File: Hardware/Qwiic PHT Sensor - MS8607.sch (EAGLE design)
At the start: 21 parts, among them J3 PTH, U1 MS8607-02BA01

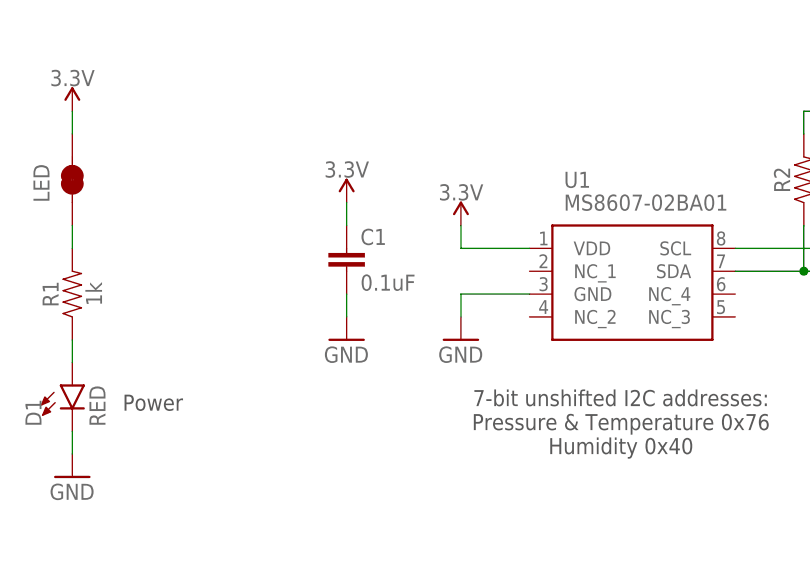
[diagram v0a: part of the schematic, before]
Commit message: Added the restrict area between the MS8607 pins
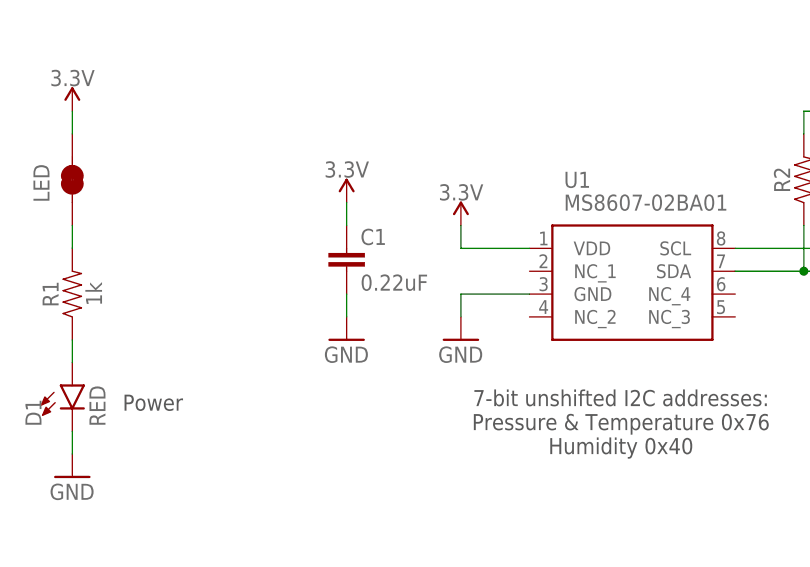
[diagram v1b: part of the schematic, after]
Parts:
- C1: value 0.1uF -> 0.22uF; device SparkFun-Capacitors:0.1UF-0603-25V-(+80/-20%) -> SparkFun-Capacitors:0.22UF-0603-25V-10%
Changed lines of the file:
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@@
 <part name="FRAME1" library="SparkFun-Aesthetics" deviceset="FRAME-LETTER" device=""/>
 <part name="U$2" library="SparkX" deviceset="SPARKX-LOGO" device="4"/>
-<part name="C1" library="SparkFun-Capacitors" deviceset="0.1UF" device="-0603-25V-(+80/-20%)" value="0.1uF"/>
+<part name="C1" library="SparkFun-Capacitors" library_urn="urn:adsk.eagle:library:510" deviceset="0.22UF" device="-0603-25V-10%" package3d_urn="urn:adsk.eagle:package:37414/1" value="0.22uF"/>
 <part name="SUPPLY8" library="SparkFun-PowerSymbols" deviceset="3.3V" device=""/>
 <part name="J1" library="SparkFun-Connectors" deviceset="I2C_STANDARD" device="QWIIC"/>
